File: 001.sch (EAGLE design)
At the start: 13 parts, among them X1 0446200002, X2 0446200002, X3 0446200002, X4 0446200002

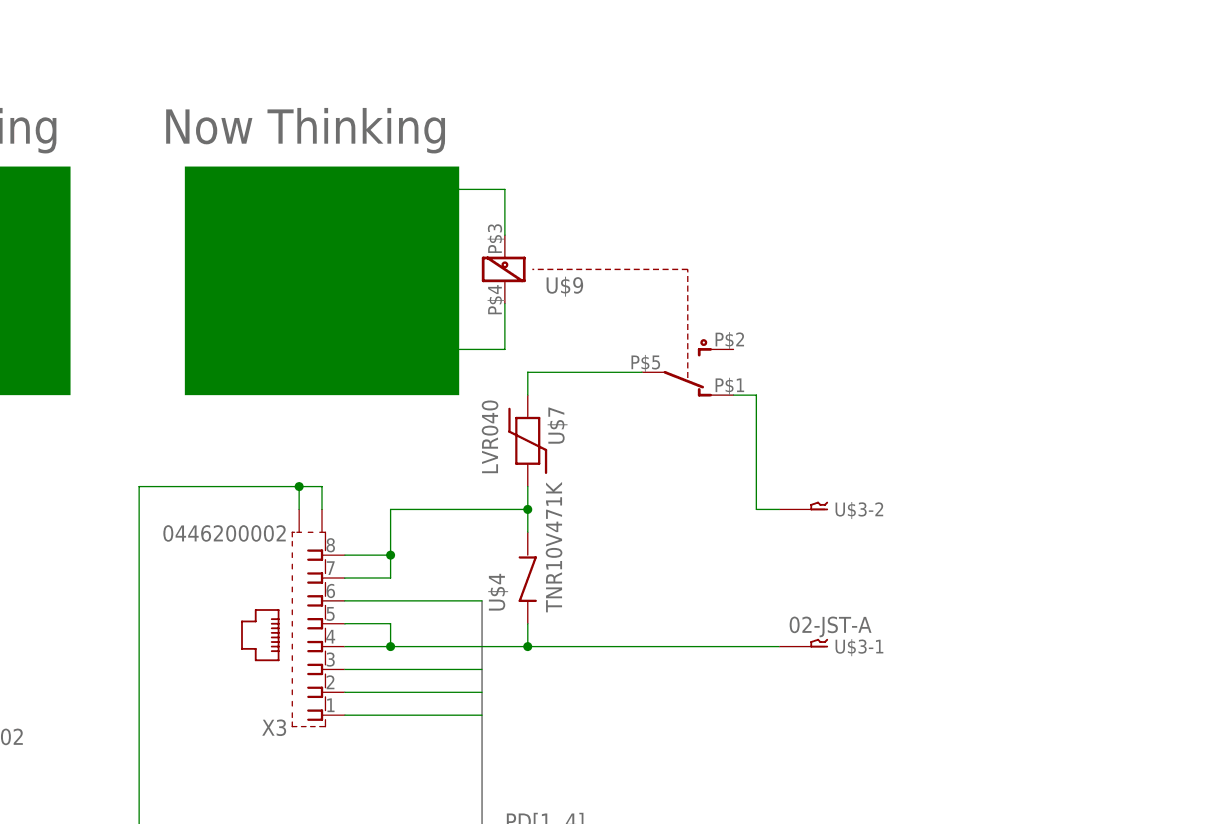
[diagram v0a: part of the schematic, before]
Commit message: リレーコイル電源を5V化する必要が有る場合にはレギュレータを入れる
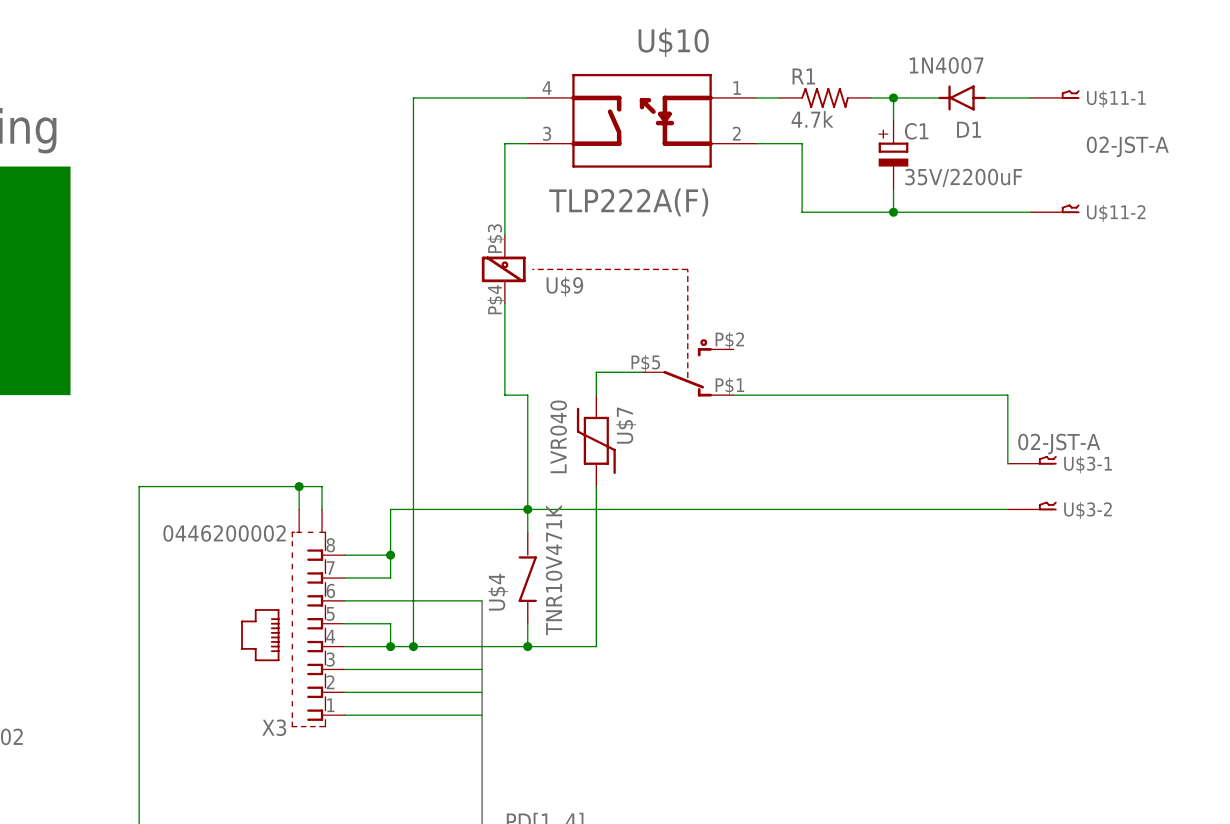
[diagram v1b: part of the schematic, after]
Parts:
- added C1: 35V/2200uF, rcl:CPOL-EUE7.5-16
- added D1: 1N4007, Diodes:1N4007
- added R1: 4.7k, rcl:R-US_0207/5V
- added U$10: (no value), Toshiba-TLP222AF:TOSHIBA_TLP222A_F_SIMPLE
- added U$11: 02-JST-A, holly:02-JST-A
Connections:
- new net N$13: C1.+, D1.C, R1.2
- new net N$14: D1.A, U$11-1.1
- new net N$15: C1.-, U$10.CATHODE, U$11-2.1
- new net VCC_PD: U$10.2_DRAIN, U$4.2, U$7.2, X3.4, X3.5
- net N$10: now also U$3-1.1; no longer U$3-2.1
- net N$12: now also R1.1, U$10.ANODE; no longer U$9.1, U$9.2
- net N$5: now also U$10.1_DRAIN, U$9.1; no longer U$3-1.1, U$4.2, X3.4, X3.5
- net N$6: now also U$3-2.1, U$9.2; no longer U$7.2
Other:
- moved on the sheet: U$3-1, U$3-2, U$7
